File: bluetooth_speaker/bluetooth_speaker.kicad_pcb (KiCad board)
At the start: 2 copper layers, 70 x 44 mm, 47 parts, among them J1 Conn_Coaxial, J2 USB_C_Receptacle_USB2.0_16P, J3 282836-4, J5 Conn_01x04_Pin, Q1 SS8050-G, Q2 SS8050-G, U1 MAX98357A, U2 XL4015, U3 CP2102N-A01-GQFN28, U4 ESP32-D0WD-V3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

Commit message: Completed the PCB design
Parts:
- moved R1 11.2 mm to (142.1, 116.4), turned to -90 degrees
- moved R10 3.68 mm to (152.7, 109.3)
- moved Q2 3.68 mm to (148.9, 108.3)
- moved C10 3.68 mm to (155.6, 106.7)
- moved Q1 3.68 mm to (152.9, 106.5)
- moved R9 3.68 mm to (148.7, 105.4)
- moved C4 2.78 mm to (134.7, 105.2)
- moved C12 0.89 mm to (172.2, 105.5)
- moved C13 0.63 mm to (175.2, 94.1)
- moved C14 0.63 mm to (173.6, 94.1)
- moved C15 0.63 mm to (172.1, 94.1)
- moved L2 0.63 mm to (172.1, 97.6)
- moved C11 0.61 mm to (163.1, 107.0)
- moved C18 0.61 mm to (164.8, 105.3)
- moved C21 0.06 mm to (156.6, 116.9)
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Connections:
- U4 pad 14: /LRCLK -> /BTN_VOL_DOWN
- U4 pad 15: /BCLK -> /BTN_VOL_UP
- U4 pad 16: /SD_MODE -> /BTN_PLAY
- U4 pad 34: /BTN_VOL_DOWN -> /SD_MODE
- U4 pad 35: /BTN_VOL_UP -> /DATA
- U4 pad 36: /BTN_PLAY -> /BCLK
- U4 pad 39: /DATA -> /LRCLK
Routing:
- net /DATA: track 2.35 -> 36.8 mm
- net /BCLK: track 3.04 -> 36.7 mm
- net /SD_MODE: track 0.00 -> 33.1 mm
- net /LRCLK: track 5.23 -> 31.3 mm, vias 0 -> 2
- net +3.3V: track 124.4 -> 149.8 mm, vias 5 -> 7
- net Net-(U3-VBUS): track 0.00 -> 17.8 mm, vias 0 -> 2
- net /USB-UART Converter/USB_D+: track 1.74 -> 14.7 mm
- net /BTN_VOL_DOWN: track 24.5 -> 12.2 mm
- net /BTN_VOL_UP: track 23.7 -> 11.5 mm
- net /BTN_PLAY: track 22.7 -> 10.8 mm
- net /USB-UART Converter/USB_D-: track 2.66 -> 13.9 mm
- net GND: track 50.4 -> 58.6 mm, vias 21 -> 92
- net Net-(J2-CC1): track 3.05 -> 8.95 mm, vias 0 -> 1
- net /USB-UART Converter/VBUS: track 7.55 -> 12.3 mm
- net /EN: track 28.1 -> 31.7 mm
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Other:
- board text added: "*"
- board text added: "+ AUDIO -"
- board text added: "+ BAT -"
- board text added: "GND"
- board text added: "PLAY"
- board text added: "VOL+"
- board text added: "VOL-"

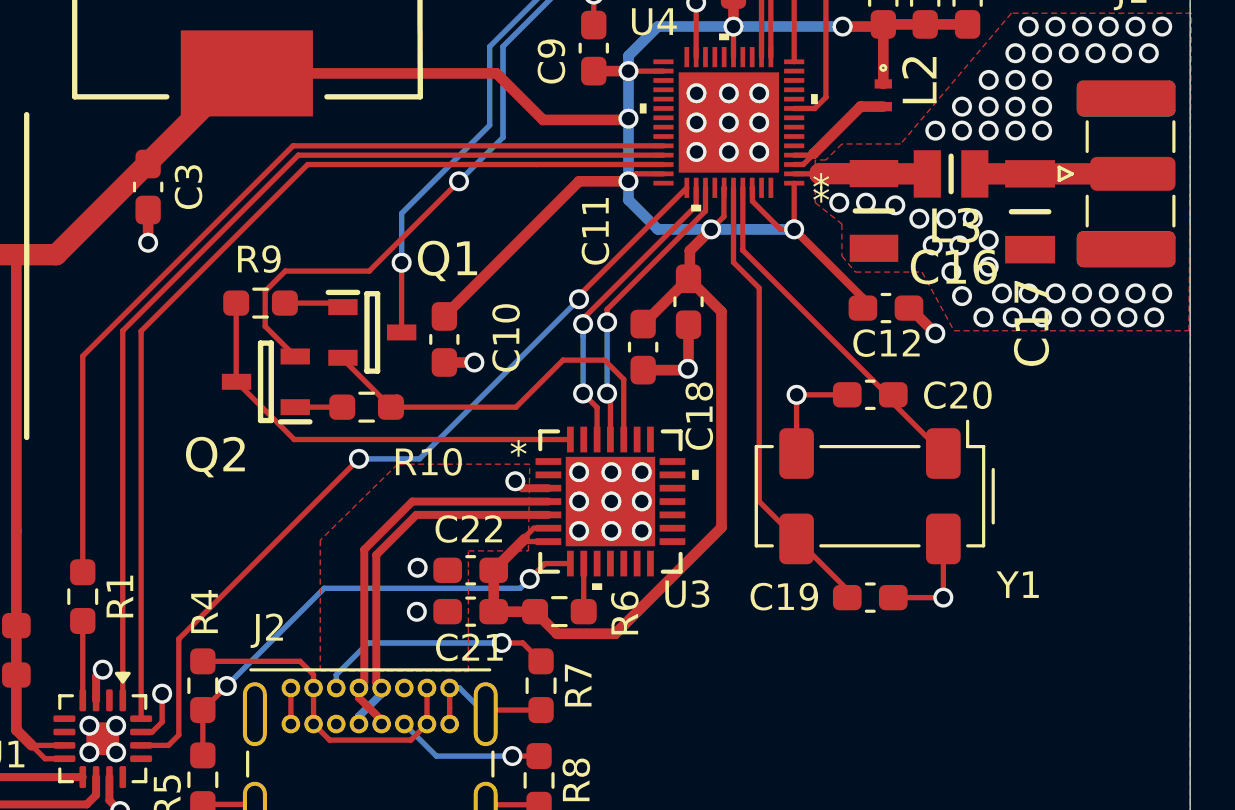
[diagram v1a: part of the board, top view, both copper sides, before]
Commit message: Exchanged CP2102N to CP2102C due to discontinuation
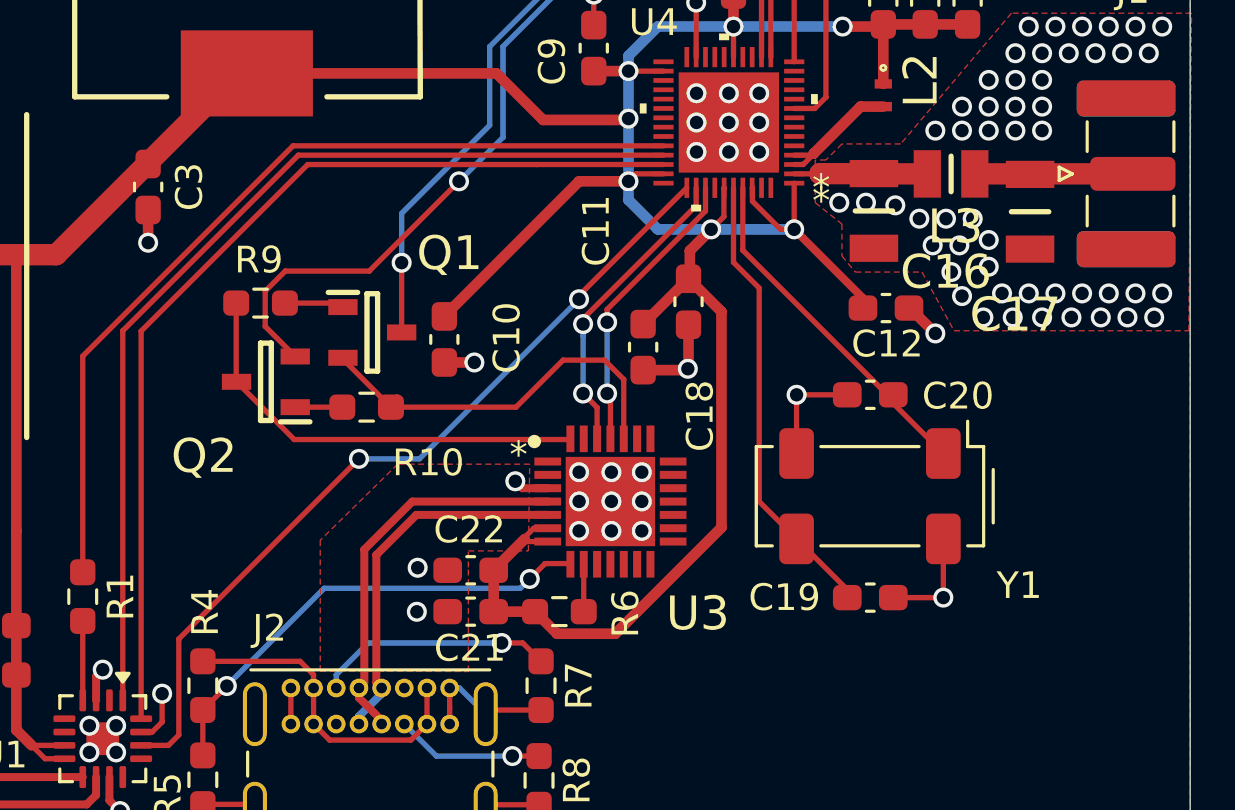
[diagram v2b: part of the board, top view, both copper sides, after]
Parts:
- C1, C13: value 10µF -> 10uF
- C10, C12, C15, C2, C22, C5: value 0.1µF -> 0.1uF
- C14, C18, C3, C6, C7, C9: value 1µF -> 1uF
- C17: footprint SamacSys_Parts:CAPC3216X170N -> SamacSys_Parts:CAPC3216X94N
- C21: value 4.7µF -> 4.7uF
- C4: value 330µF/25V -> 330uF/25V
- C8: value 220µF/50V -> 220uF/50V
- L1: value 47µH/5A -> 47uH/5A
- R1: value 300kΩ -> 300k
- R2: value 16.5kΩ -> 16.5k
- R3: value 10kΩ -> 10k
- R4: value 22.1kΩ -> 22.1k
- R5: value 47.5kΩ -> 47.5k
- R6: value 1kΩ -> 1k
- U3: value CP2102N-A01-GQFN28 -> CP2102C-A01-GQFN28; footprint CP2102N-A01-GQFN28:QFN28_5X5_SIL -> SamacSys_Parts:QFN50P500X500X80-29N-D

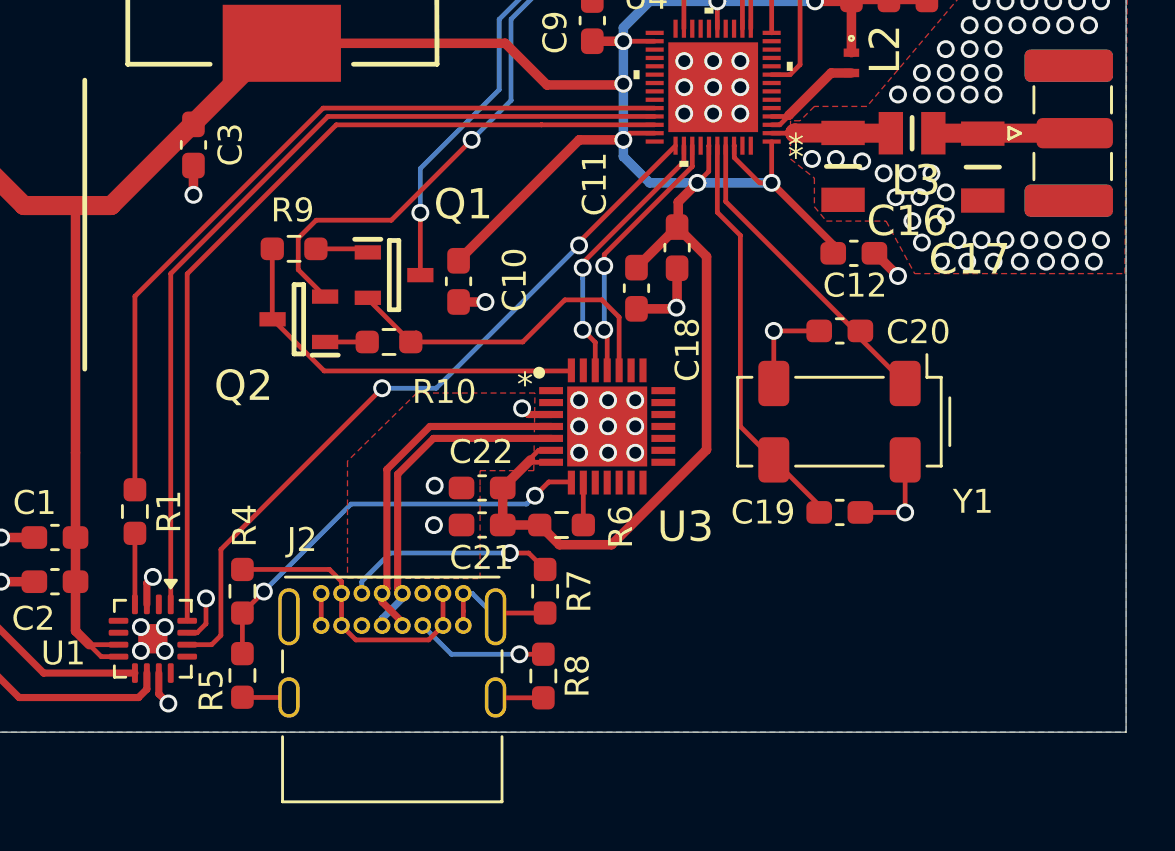
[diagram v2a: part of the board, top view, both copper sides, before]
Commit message: Updated crystal design
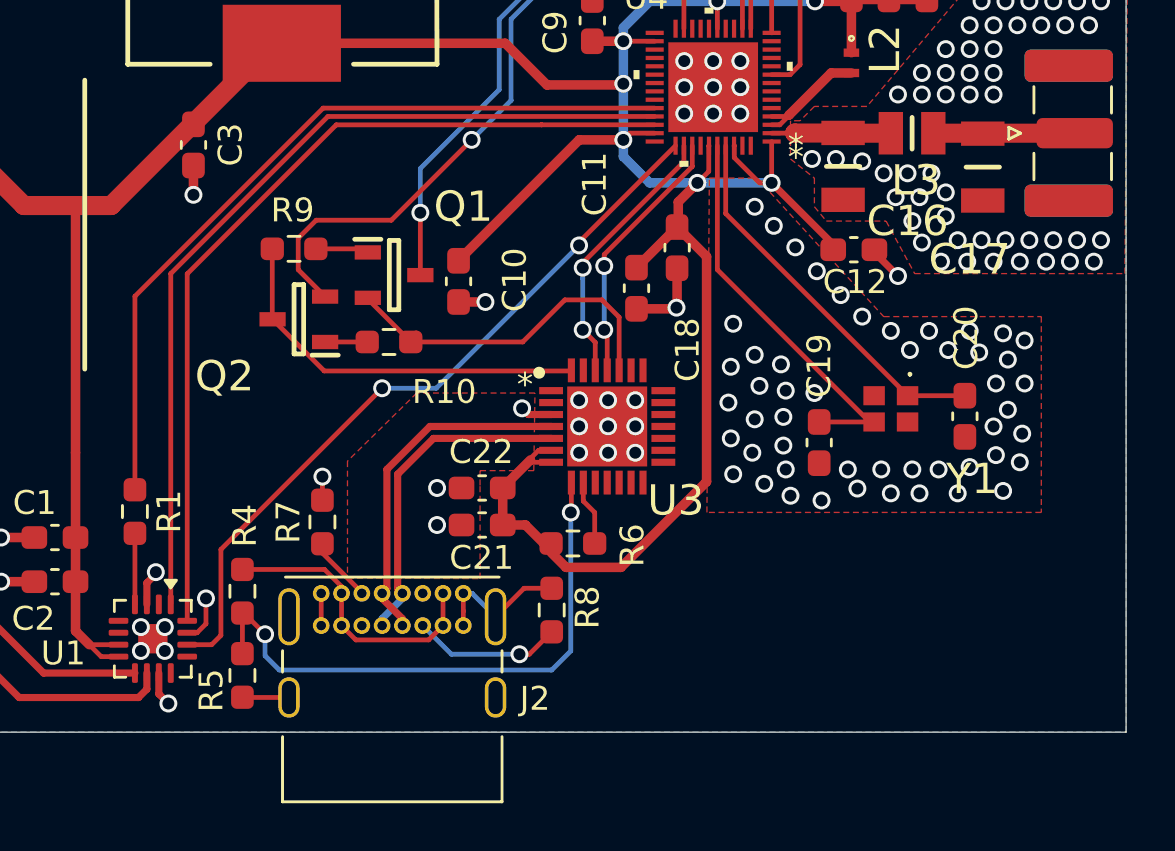
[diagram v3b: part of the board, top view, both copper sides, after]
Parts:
- Y1: footprint Crystal:Crystal_SMD_SeikoEpson_MC306-4Pin_8.0x3.2mm -> SamacSys_Parts:FW400WFMR1
- moved R7 9.77 mm to (149.9, 116.8), turned to 90 degrees
- moved C20 6.34 mm to (176.8, 112.4), turned to 90 degrees
- moved C19 3.05 mm to (170.7, 113.5), turned to -90 degrees
- moved R8 2.78 mm to (159.5, 120.5), turned to 90 degrees
- moved Y1 2.22 mm to (173.7, 112.1)
- moved R6 0.91 mm to (160.4, 117.7)
- moved C12 0.15 mm to (172.2, 105.4)
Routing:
- net GND: track 58.6 -> 50.4 mm, vias 92 -> 141
- net Net-(U3-VBUS): track 17.8 -> 24.4 mm
- net Net-(J2-CC1): track 8.95 -> 2.76 mm, vias 1 -> 0
- net /XTAL_P: track 13.2 -> 16.0 mm
- net +3.3V: track 149.8 -> 151.2 mm
- net Net-(U3-RSTB): track 1.80 -> 2.77 mm
- net Net-(J2-CC2): track 5.62 -> 6.36 mm
- net /XTAL_N: track 17.1 -> 16.5 mm
